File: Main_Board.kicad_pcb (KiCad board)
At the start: 2 copper layers, 90 x 90 mm, 64 parts, among them J1 DAC_12-bits, J2 Bias_Header, J3 Measurement_Header, Q1 Q_PNP_BCE, Q2 Q_NPN_BCE, U1 AD667, U2 LF356, U3 AD558JN

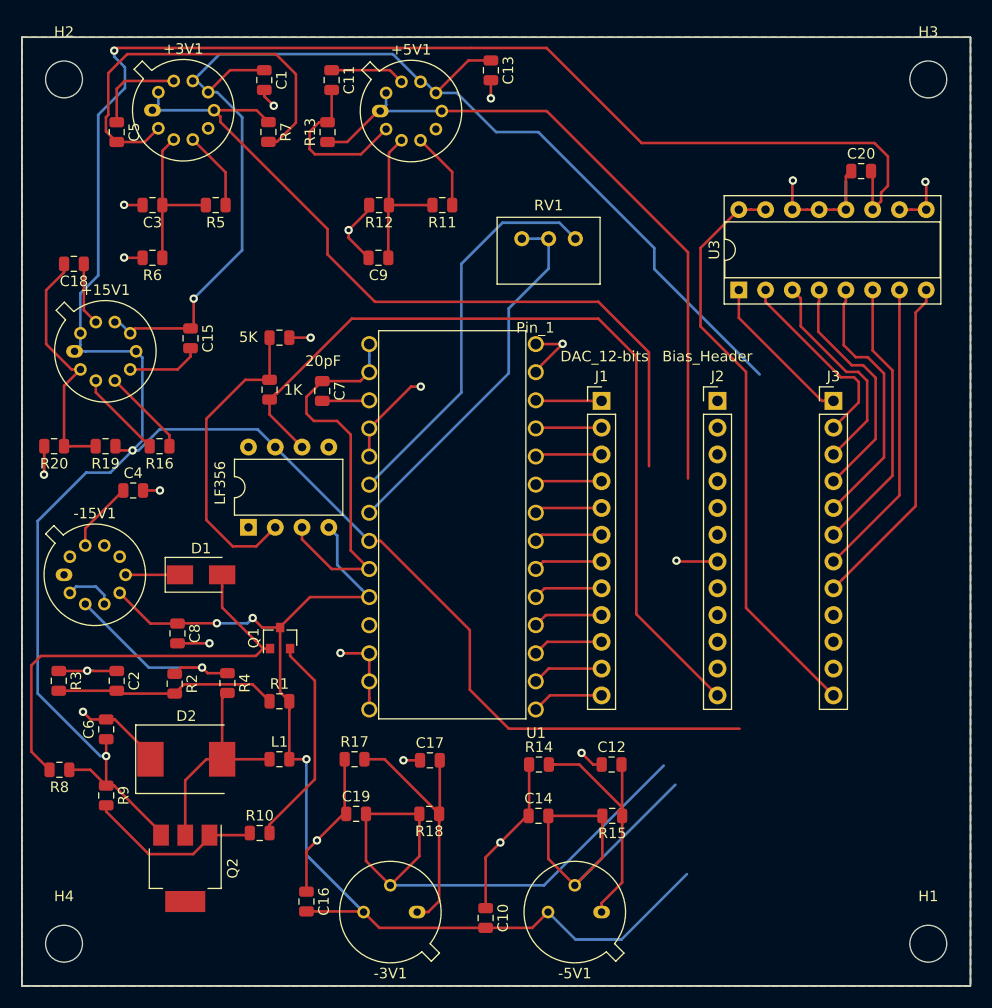
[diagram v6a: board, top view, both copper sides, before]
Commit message: Got rid of 8-bit DAC
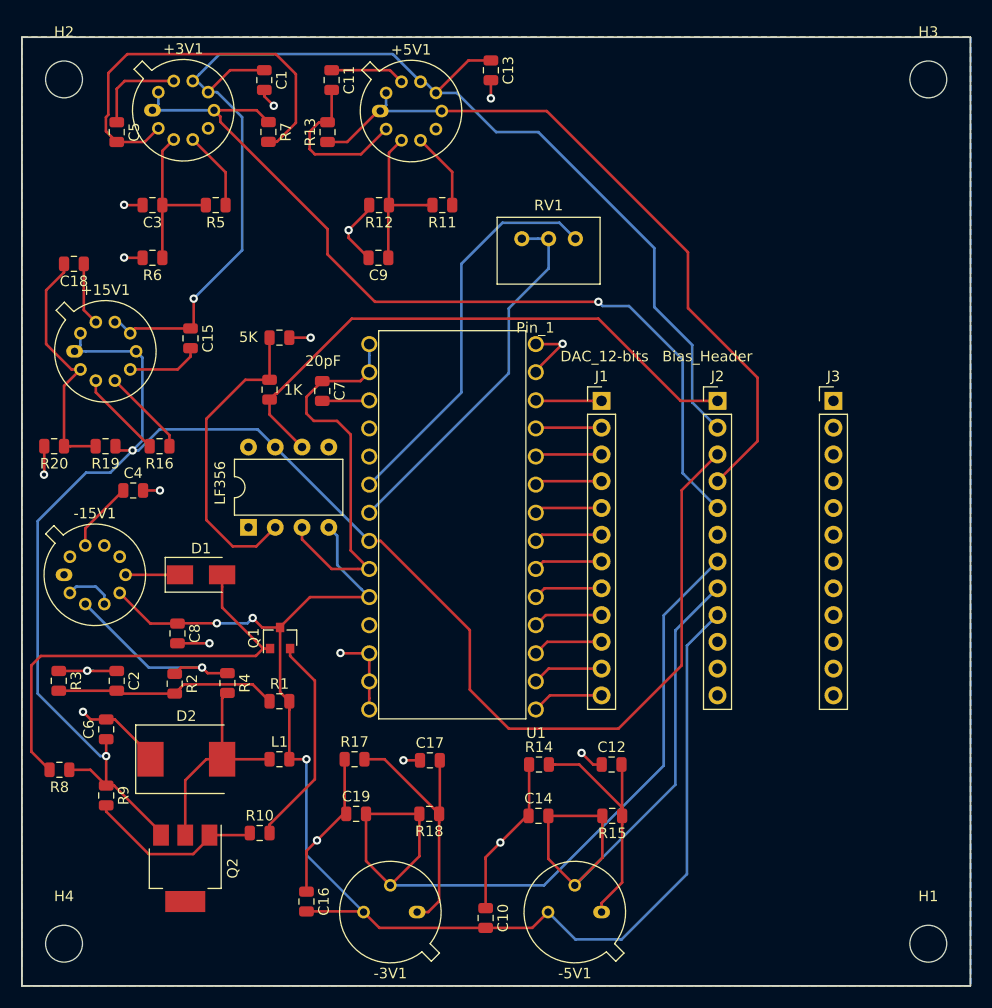
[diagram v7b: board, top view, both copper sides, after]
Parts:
- removed C20: 0.1u, Capacitor_SMD:C_0805_2012Metric
- removed U3: AD558JN, Package_DIP:DIP-16_W7.62mm_Socket
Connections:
- J2 pad 1: /-200V -> /GridStack
- J2 pad 10: /+15V -> Net-(J2-Pad10)
- J2 pad 11: /Vin -> Net-(J2-Pad11)
- J2 pad 12: /GridStack -> /-200V
- J2 pad 2: Net-(J2-Pad2) -> /Vin
- J2 pad 3: Net-(J2-Pad3) -> /+15V
- J2 pad 4: /-15V -> /+5V
- J2 pad 5: /-5V -> /+3V
- J2 pad 6: /-3V -> GND
- J2 pad 7: GND -> /-3V
- J2 pad 8: /+3V -> /-5V
- J2 pad 9: /+5V -> /-15V
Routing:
- net /+15V: track 262.2 -> 164.4 mm, vias 3 -> 2
- net /MSP430_P2.6_transistorBaseVoltage: track 55.4 -> 0.00 mm
- net GND: track 125.6 -> 92.8 mm, vias 21 -> 17
- net /MSP430_P3.3_Bit7: track 31.9 -> 0.00 mm
- net /MSP430_P3.2_Bit6: track 28.4 -> 0.00 mm
- net /MSP430_P3.1_Bit5: track 26.3 -> 0.00 mm
- net /GridStack: track 80.6 -> 54.7 mm
- net /-15V: track 107.1 -> 132.9 mm
- net /MSP430_P3.0_Bit4: track 25.0 -> 0.00 mm
- net /MSP430_P2.7_Bit3: track 22.7 -> 0.00 mm
- net /-3V: track 51.4 -> 72.8 mm
- net /MSP430_P2.6_Bit2: track 20.5 -> 0.00 mm
- net /-5V: track 33.9 -> 54.2 mm
- net /MSP430_P2.5_Bit1: track 18.4 -> 0.00 mm
- net /MSP430_P2.4_Bit0: track 14.9 -> 0.00 mm
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
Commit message: Fin
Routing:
- removed copper zone on B.Cu, net GND
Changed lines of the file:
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@@
   (segment (start 35.5 115.375) (end 36.056237 114.818763) (width 0.25) (layer F.Cu) (net 50))
   (segment (start 36.056237 114.818763) (end 36.181237 114.818763) (width 0.25) (layer F.Cu) (net 50))
-  (zone (net 1) (net_name GND) (layer B.Cu) (hatch edge 0.508)
-    (connect_pads (clearance 0.508))
-    (min_thickness 0.254)
-    (fill (arc_segments 32) (thermal_gap 0.508) (thermal_bridge_width 0.508))
-    (polygon
-      (pts
-        (xy 12 81) (xy 102 81) (xy 102 171) (xy 12 171)
-      )
-    )
-  )
-  (zone (net 1) (net_name GND) (layer B.Cu) (hatch edge 0.508)
-    (connect_pads (clearance 0.508))
-    (min_thickness 0.254)
-    (fill (arc_segments 32) (thermal_gap 0.508) (thermal_bridge_width 0.508))
-    (polygon
-      (pts
-        (xy 12 81) (xy 102 81) (xy 102 171) (xy 12 171)
-      )
-    )
-  )
-  (zone (net 1) (net_name GND) (layer B.Cu) (hatch edge 0.508)
-    (connect_pads (clearance 0.508))
-    (min_thickness 0.254)
-    (fill (arc_segments 32) (thermal_gap 0.508) (thermal_bridge_width 0.508))
-    (polygon
-      (pts
-        (xy 12 81) (xy 102 81) (xy 102 171) (xy 12 171)
-      )
-    )
-  )
-  (zone (net 1) (net_name GND) (layer B.Cu) (hatch edge 0.508)
-    (connect_pads (clearance 0.508))
-    (min_thickness 0.254)
-    (fill (arc_segments 32) (thermal_gap 0.508) (thermal_bridge_width 0.508))
-    (polygon
-      (pts
-        (xy 102.043 171.043) (xy 12 171.043) (xy 12 81) (xy 102.043 81)
-      )
-    )
-  )
 )
